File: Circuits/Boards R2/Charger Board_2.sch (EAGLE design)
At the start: 80 parts, among them CON1 ISP(2X3), CON10 HEADER_3X1, CON11 HEADER_3X1, CON12 HEADER_3X1, CON13 HEADER_4X1, CON2 SCREWTERMINAL_1X2, CON3 HEADER_3X1, CON4 HEADER_3X1, CON5 HEADER_3X1, CON6 HEADER_3X1, CON7 HEADER_3X1, CON8 HEADER_3X1, CON9 HEADER_3X1, IC1 NCP1117DT33G, T1 NPN2N2222, T2 NPN2N2222, T3 SI4421DY, U1 ATMEGA324P, U2 ACS711, U3 JOYSTICKPTH, U4 MX25L25735E

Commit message: 
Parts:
- added CON14, CON15: HEADER_3X1, Mechanical:HEADER_3X1
- B1: value PIEZOBUZZER -> PIEZOBUZZERPTH; device Passive:PIEZOBUZZER -> Passive:PIEZOBUZZERPTH
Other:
- moved on the sheet: B1
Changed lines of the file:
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@@
 <part name="CON1" library="Mechanical" deviceset="ISP" device="(2X3)"/>
 <part name="GND5" library="Supply" deviceset="GND" device=""/>
-<part name="B1" library="Passive" deviceset="PIEZOBUZZER" device=""/>
 <part name="R8" library="Passive" deviceset="RES" device="0603" value="1k"/>
 <part name="GND6" library="Supply" deviceset="GND" device=""/>
@@
 <part name="R24" library="Passive" deviceset="RES" device="0603" value="10k"/>
 <part name="P+5" library="Supply" deviceset="+5V" device=""/>
+<part name="CON14" library="Mechanical" deviceset="HEADER_3X1" device=""/>
+<part name="CON15" library="Mechanical" deviceset="HEADER_3X1" device=""/>
+<part name="B1" library="Passive" deviceset="PIEZOBUZZER" device="PTH"/>
 </parts>
 <sheets>
@@
 <instance part="CON1" gate="G$1" x="-165.1" y="-15.24"/>
 <instance part="GND5" gate="1" x="147.32" y="-30.48"/>
-<instance part="B1" gate="G$1" x="-172.72" y="-53.34"/>
 <instance part="R8" gate="G$1" x="-185.42" y="-53.34" rot="R90"/>
 <instance part="GND6" gate="1" x="-185.42" y="-78.74"/>
@@
 <instance part="R24" gate="G$1" x="-71.12" y="-68.58" rot="R90"/>
 <instance part="P+5" gate="1" x="-71.12" y="-58.42"/>
+<instance part="CON14" gate="G$1" x="88.9" y="25.4"/>
+<instance part="CON15" gate="G$1" x="195.58" y="104.14"/>
+<instance part="B1" gate="G$1" x="-172.72" y="-53.34"/>
 </instances>
 <busses>
@@
 <net name="N$9" class="0">
 <segment>
-<pinref part="B1" gate="G$1" pin="-"/>
 <wire x1="-177.8" y1="-53.34" x2="-177.8" y2="-60.96" width="0.1524" layer="91"/>
 <wire x1="-177.8" y1="-60.96" x2="-185.42" y2="-60.96" width="0.1524" layer="91"/>
@@
 <wire x1="-185.42" y1="-60.96" x2="-185.42" y2="-63.5" width="0.1524" layer="91"/>
 <pinref part="T1" gate="G$1" pin="C"/>
+<pinref part="B1" gate="G$1" pin="-"/>
 </segment>
 </net>
@@
 <pinref part="R8" gate="G$1" pin="2"/>
 <wire x1="-185.42" y1="-43.18" x2="-185.42" y2="-45.72" width="0.1524" layer="91"/>
-<pinref part="B1" gate="G$1" pin="+"/>
 <wire x1="-185.42" y1="-45.72" x2="-185.42" y2="-48.26" width="0.1524" layer="91"/>
 <wire x1="-185.42" y1="-45.72" x2="-177.8" y2="-45.72" width="0.1524" layer="91"/>
@@
 <junction x="-185.42" y="-45.72"/>
 <pinref part="+3V5" gate="G$1" pin="+3V3"/>
-</segment>
-<segment>
+<pinref part="B1" gate="G$1" pin="+"/>
+</segment>
+<segment>

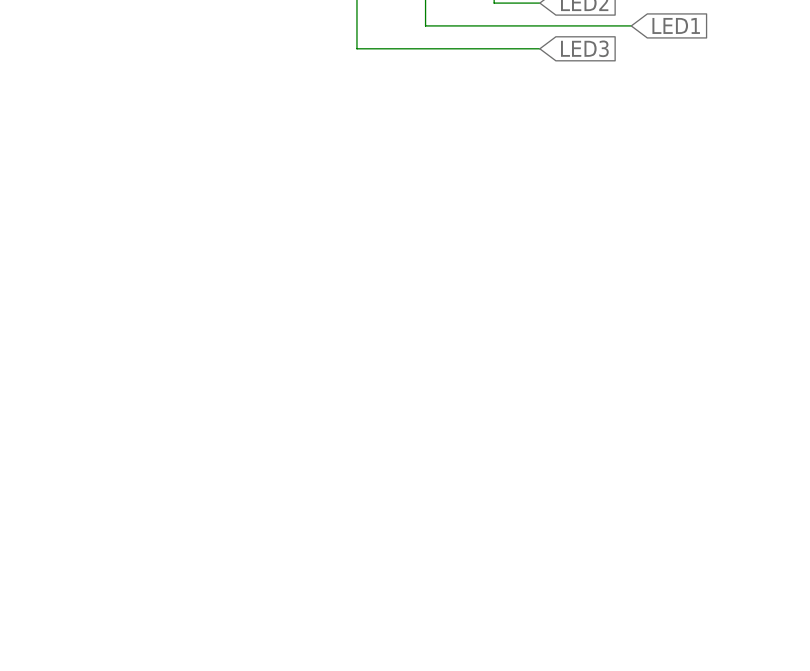
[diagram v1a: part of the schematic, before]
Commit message: started adding rgb edge lighting hardware
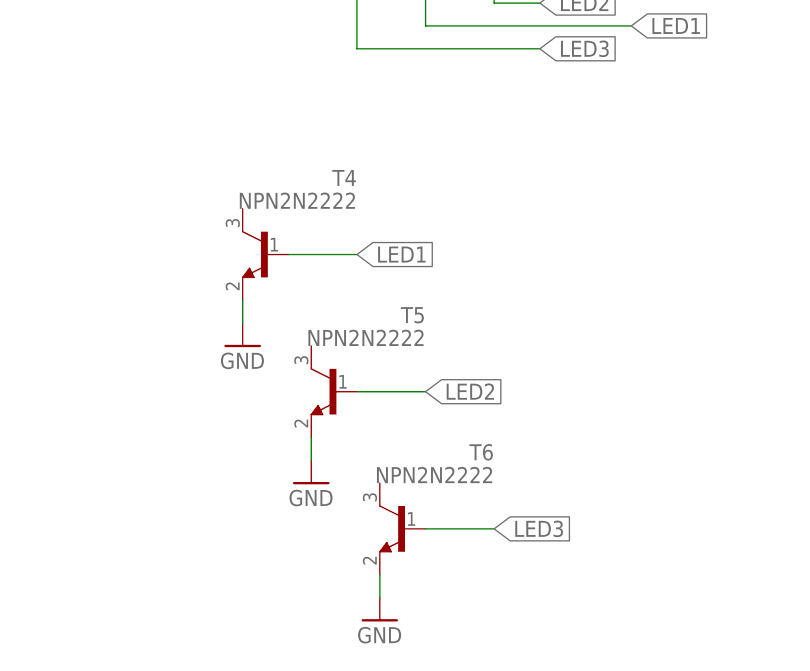
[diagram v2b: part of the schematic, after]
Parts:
- added T4, T5, T6: NPN2N2222, Passive:NPN2N2222
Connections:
- net GND: now also T4.E, T5.E, T6.E
- net LED1: now also T4.B
- net LED2: now also T5.B
- net LED3: now also T6.B
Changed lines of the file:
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@@
 <part name="CON15" library="Mechanical" deviceset="HEADER_3X1" device=""/>
 <part name="B1" library="Passive" deviceset="PIEZOBUZZER" device="PTH"/>
+<part name="T4" library="Passive" deviceset="NPN2N2222" device=""/>
+<part name="T5" library="Passive" deviceset="NPN2N2222" device=""/>
+<part name="T6" library="Passive" deviceset="NPN2N2222" device=""/>
+<part name="GND18" library="Supply" deviceset="GND" device=""/>
+<part name="GND19" library="Supply" deviceset="GND" device=""/>
+<part name="GND20" library="Supply" deviceset="GND" device=""/>
 </parts>
 <sheets>
@@
 <instance part="CON15" gate="G$1" x="195.58" y="104.14"/>
 <instance part="B1" gate="G$1" x="-172.72" y="-53.34"/>
+<instance part="T4" gate="G$1" x="-160.02" y="-144.78" rot="MR0"/>
+<instance part="T5" gate="G$1" x="-152.4" y="-160.02" rot="MR0"/>
+<instance part="T6" gate="G$1" x="-144.78" y="-175.26" rot="MR0"/>
+<instance part="GND18" gate="1" x="-162.56" y="-154.94"/>
+<instance part="GND19" gate="1" x="-154.94" y="-170.18"/>
+<instance part="GND20" gate="1" x="-147.32" y="-185.42"/>
 </instances>
 <busses>
@@
 <pinref part="GND17" gate="1" pin="GND"/>
 </segment>
+<segment>
+<pinref part="T4" gate="G$1" pin="E"/>
+<pinref part="GND18" gate="1" pin="GND"/>
+<wire x1="-162.56" y1="-152.4" x2="-162.56" y2="-149.86" width="0.1524" layer="91"/>
+</segment>
+<segment>
+<pinref part="T5" gate="G$1" pin="E"/>
+<pinref part="GND19" gate="1" pin="GND"/>
+<wire x1="-154.94" y1="-167.64" x2="-154.94" y2="-165.1" width="0.1524" layer="91"/>
+</segment>
+<segment>
+<pinref part="T6" gate="G$1" pin="E"/>
+<pinref part="GND20" gate="1" pin="GND"/>
+<wire x1="-147.32" y1="-182.88" x2="-147.32" y2="-180.34" width="0.1524" layer="91"/>
+</segment>
 </net>
 <net name="RESET" class="0">
@@
 <label x="-119.38" y="-119.38" size="1.778" layer="91" xref="yes"/>
 </segment>
+<segment>
+<pinref part="T4" gate="G$1" pin="B"/>
+<wire x1="-157.48" y1="-144.78" x2="-149.86" y2="-144.78" width="0.1524" layer="91"/>
+<label x="-149.86" y="-144.78" size="1.778" layer="91" xref="yes"/>
+</segment>
 </net>
 <net name="LED2" class="0">
@@
 <wire x1="-134.62" y1="-116.84" x2="-129.54" y2="-116.84" width="0.1524" layer="91"/>
 <label x="-129.54" y="-116.84" size="1.778" layer="91" xref="yes"/>
+</segment>
+<segment>
+<pinref part="T5" gate="G$1" pin="B"/>
+<wire x1="-149.86" y1="-160.02" x2="-142.24" y2="-160.02" width="0.1524" layer="91"/>
+<label x="-142.24" y="-160.02" size="1.778" layer="91" xref="yes"/>
 </segment>
 </net>
@@
 <label x="48.26" y="7.62" size="1.778" layer="91" xref="yes"/>
 </segment>
-</net>
+<segment>
+<pinref part="T6" gate="G$1" pin="B"/>
+<wire x1="-142.24" y1="-175.26" x2="-134.62" y2="-175.26" width="0.1524" layer="91"/>
+<label x="-134.62" y="-175.26" size="1.778" layer="91" xref="yes"/>
+</segment>
+</net>

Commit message: 
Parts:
- removed U$1, U$2: FTDI_3PIN, Mechanical:FTDI_3PIN
- added C16, C19: 10uf, Passive:CAP0805
- added C17, C18, C20, C21: .1uf, Passive:CAP0603
- added CON16: HEADER_4X1, Mechanical:HEADER_4X1
- added CON17, CON18: HEADER_3X1, Mechanical:HEADER_3X1
- added H5, H6, H7: MOUNTINGHOLE, Mechanical:MOUNTINGHOLE
- added LED7: IR, Passive:LED5MMRA
- added R25: 18, Passive:RES0603
- added R26, R29, R30: 1k, Passive:RES0603
- added T7, T8, T9: NPN2N2222, Passive:NPN2N2222
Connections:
- new net BLUE: CON16.1, T7.C
- new net GREEN: CON16.2, T8.C
- new net N$18: R26.1, T4.C, T7.B
- new net N$2: CON15.1, R16.1
- new net N$20: R29.1, T5.C, T8.B
- new net N$21: R30.1, T6.C, T9.B
- new net N$3: C12.1, C2.1, C6.1, C7.1, C8.1, C9.1, CON15.2, LED2.A, LED3.A, LED4.A, LED5.A, LED6.A, LED7.A
- new net N$5: C12.2, C2.2, C6.2, C7.2, C8.2, C9.2, CON15.3, T2.E
- new net N$6: LED7.C, R25.2
- new net RED: CON16.3, T9.C
- net +3V3: now also C16.1, C17.1, C18.1, C19.1, C20.1, C21.1, CON14.2
- net +5V: now also CON16.4, R26.2, R29.2, R30.2; no longer C12.1, C2.1, C6.1, C7.1, C8.1, C9.1, LED2.A, LED3.A, LED4.A, LED5.A, LED6.A
- net GND: now also C16.2, C17.2, C18.2, C19.2, C20.2, C21.2, CON14.3, CON17.1, CON18.1, T7.E, T8.E, T9.E; no longer C12.2, C2.2, C6.2, C7.2, C8.2, C9.2, T2.E, U$1.GND, U$2.GND
- net N$10: now also R25.1
- net N$19: now also CON18.3; no longer U$2.RXI
- net N$4: now also CON18.2; no longer U$2.TXO
- net N$7: now also CON17.3; no longer U$1.RXI
- net N$8: now also CON17.2; no longer U$1.TXO
- net TRANSMITLEDS: now also CON14.1; no longer R16.1
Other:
- moved on the sheet: CON14, CON15, LED10, R24, R27, T3, T5, T6, U$3, U$4

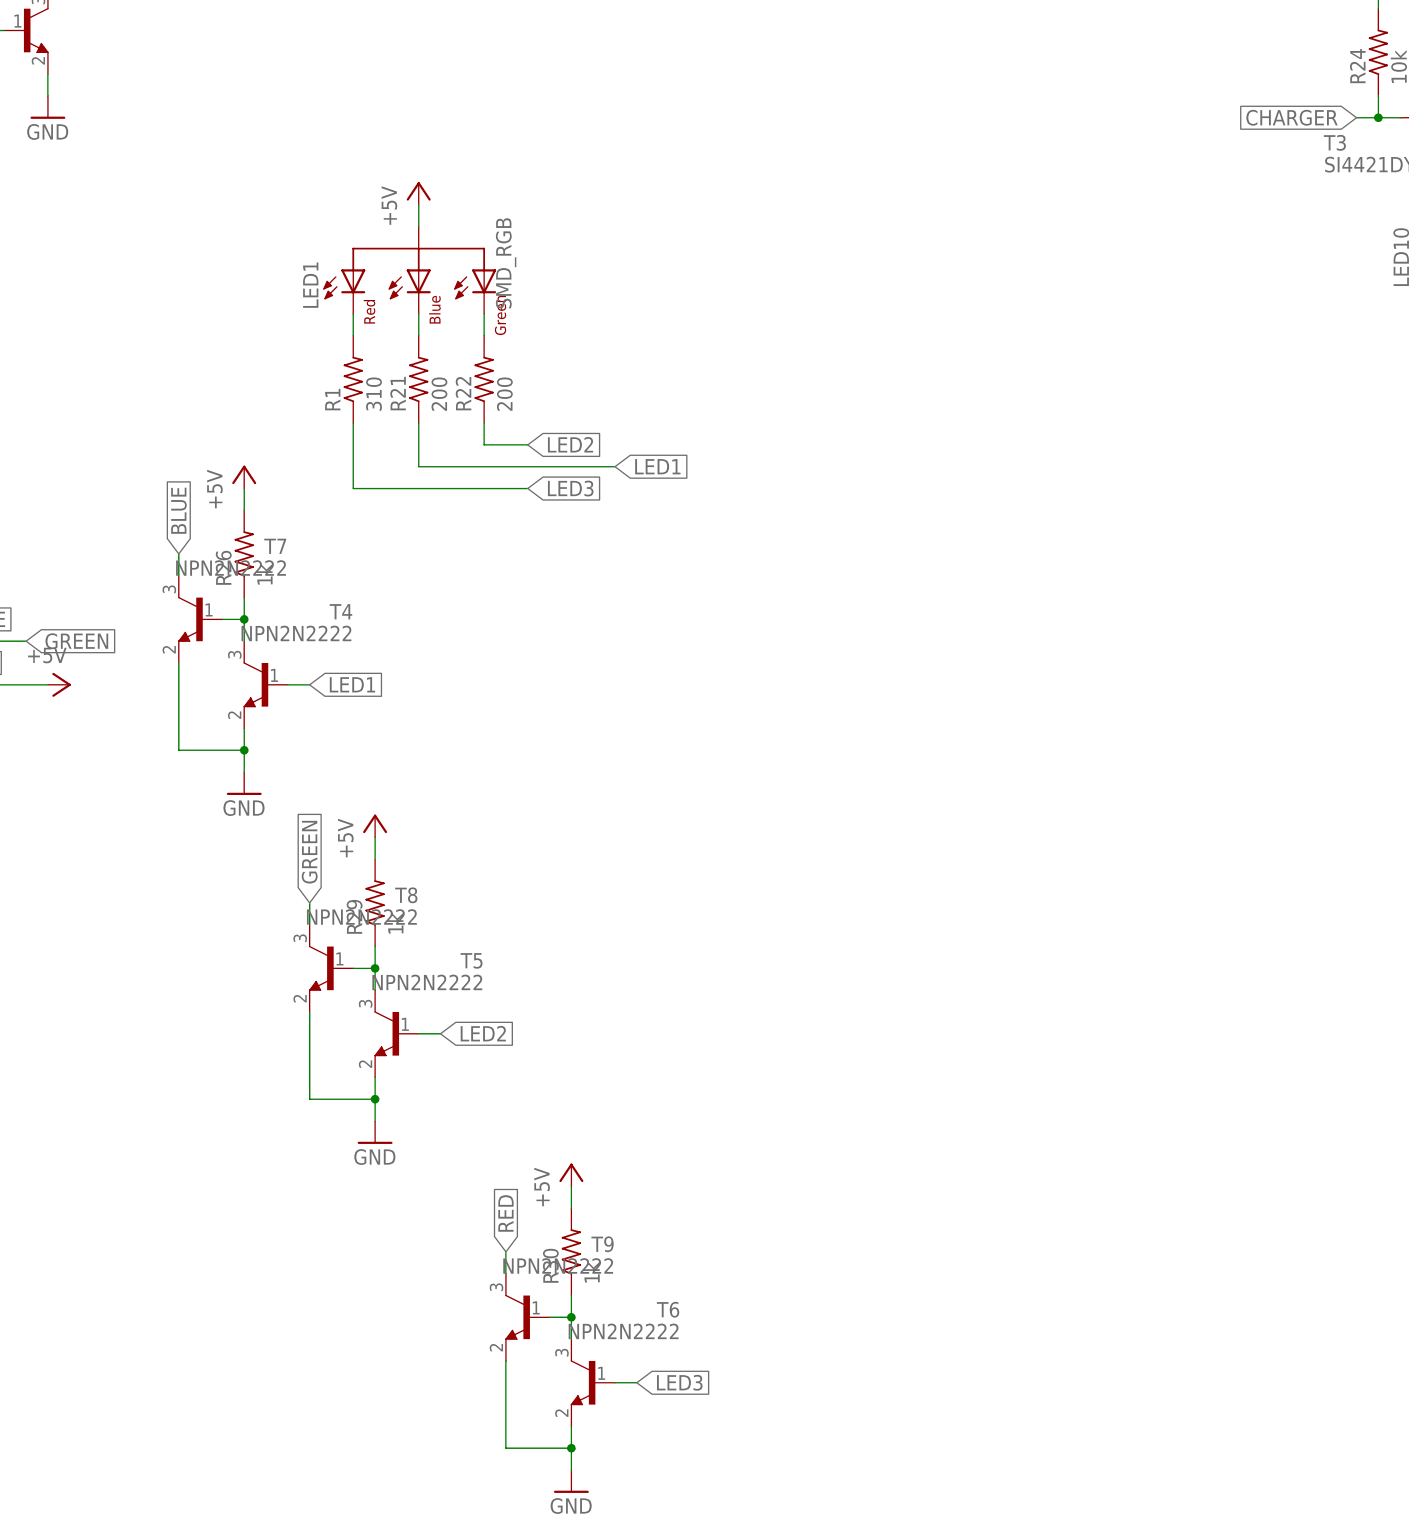
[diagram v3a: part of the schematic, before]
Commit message: 
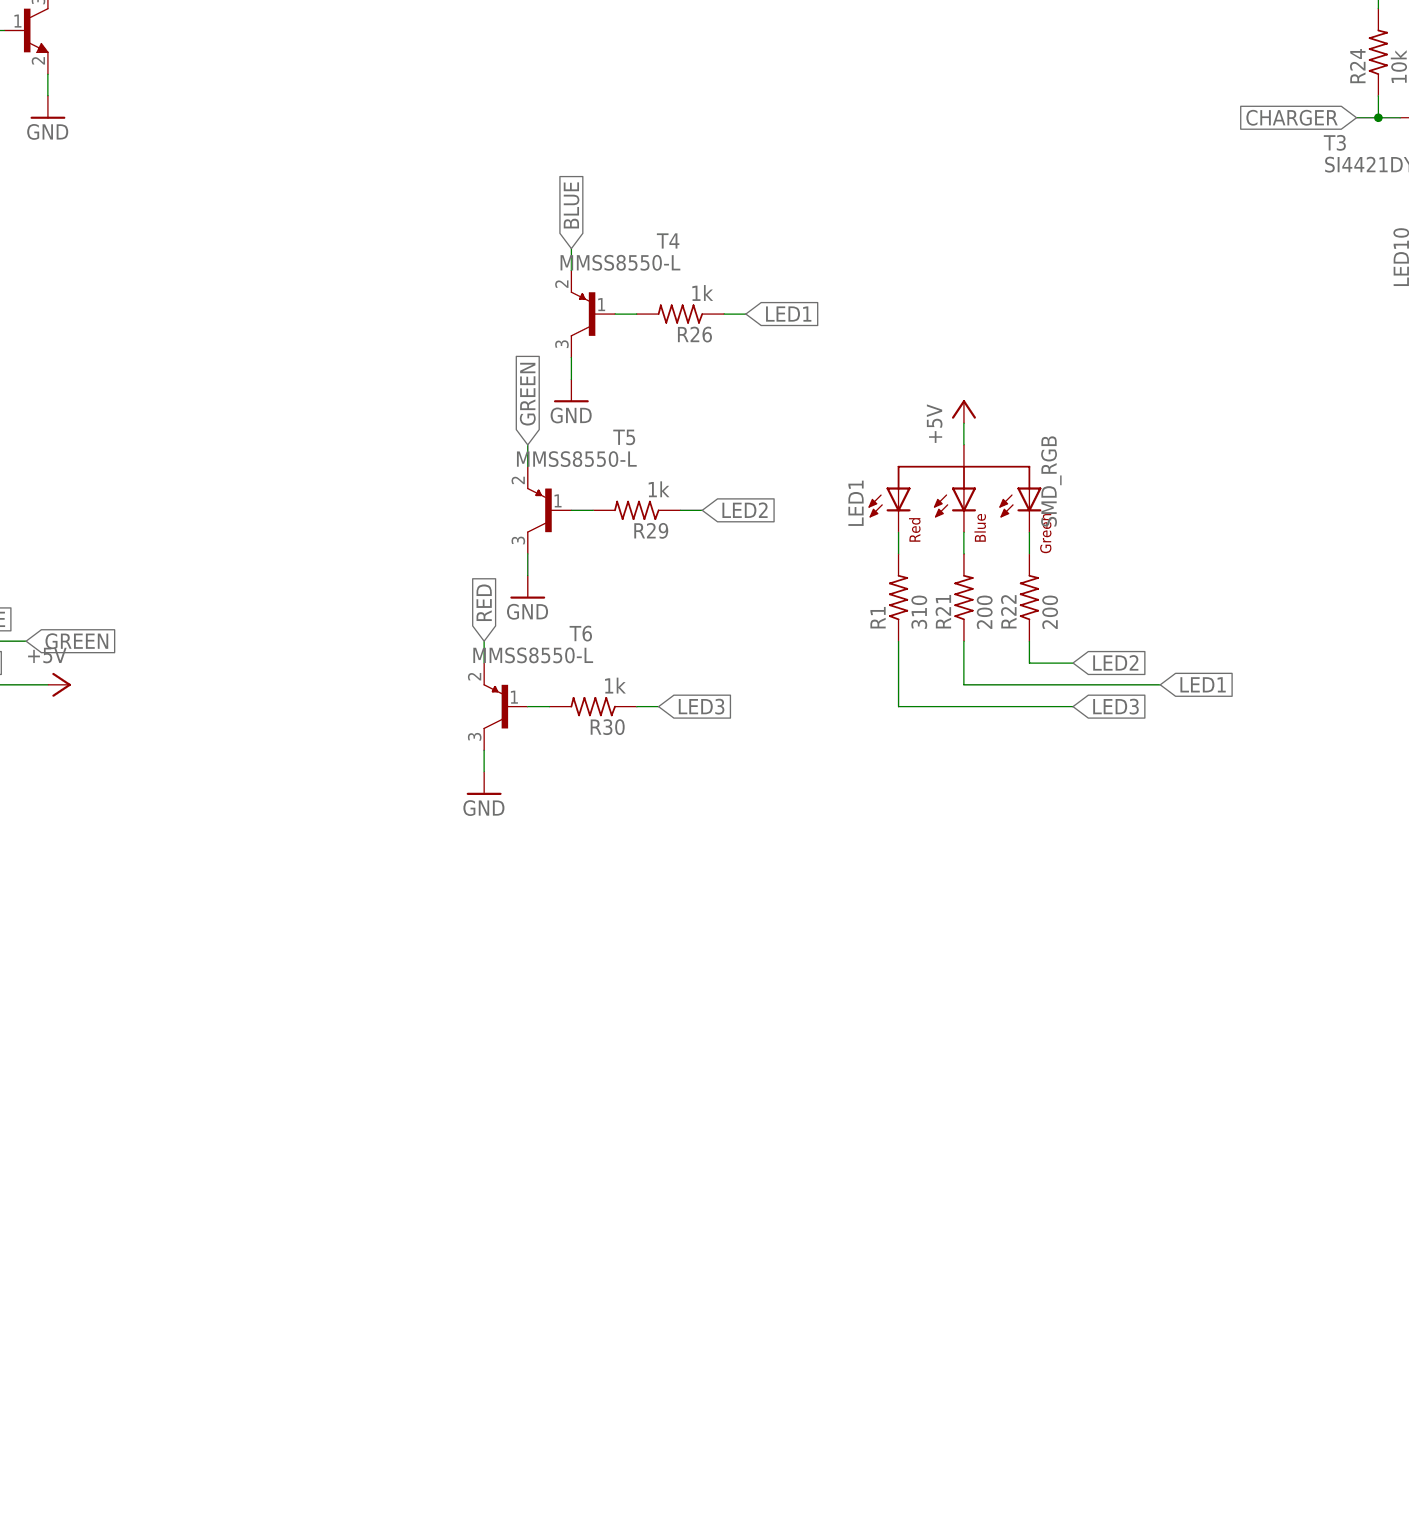
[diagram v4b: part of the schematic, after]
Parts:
- removed T7, T8, T9: NPN2N2222, Passive:NPN2N2222
- T4, T5, T6: value NPN2N2222 -> MMSS8550-L; device Passive:NPN2N2222 -> Passive:MMSS8550-L
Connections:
- removed net N$18: R26.1, T4.C, T7.B
- removed net N$20: R29.1, T5.C, T8.B
- removed net N$21: R30.1, T6.C, T9.B
- new net N$36: R26.2, T4.B
- new net N$40: R29.2, T5.B
- new net N$41: R30.2, T6.B
- net +5V: no longer R26.2, R29.2, R30.2
- net BLUE: now also T4.E; no longer T7.C
- net GND: now also T4.C, T5.C, T6.C; no longer T4.E, T5.E, T6.E, T7.E, T8.E, T9.E
- net GREEN: now also T5.E; no longer T8.C
- net LED1: now also R26.1; no longer T4.B
- net LED2: now also R29.1; no longer T5.B
- net LED3: now also R30.1; no longer T6.B
- net RED: now also T6.E; no longer T9.C
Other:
- moved on the sheet: LED1, R1, R21, R22, R26, R29, R30
